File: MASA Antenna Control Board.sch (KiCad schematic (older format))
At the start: 10 parts

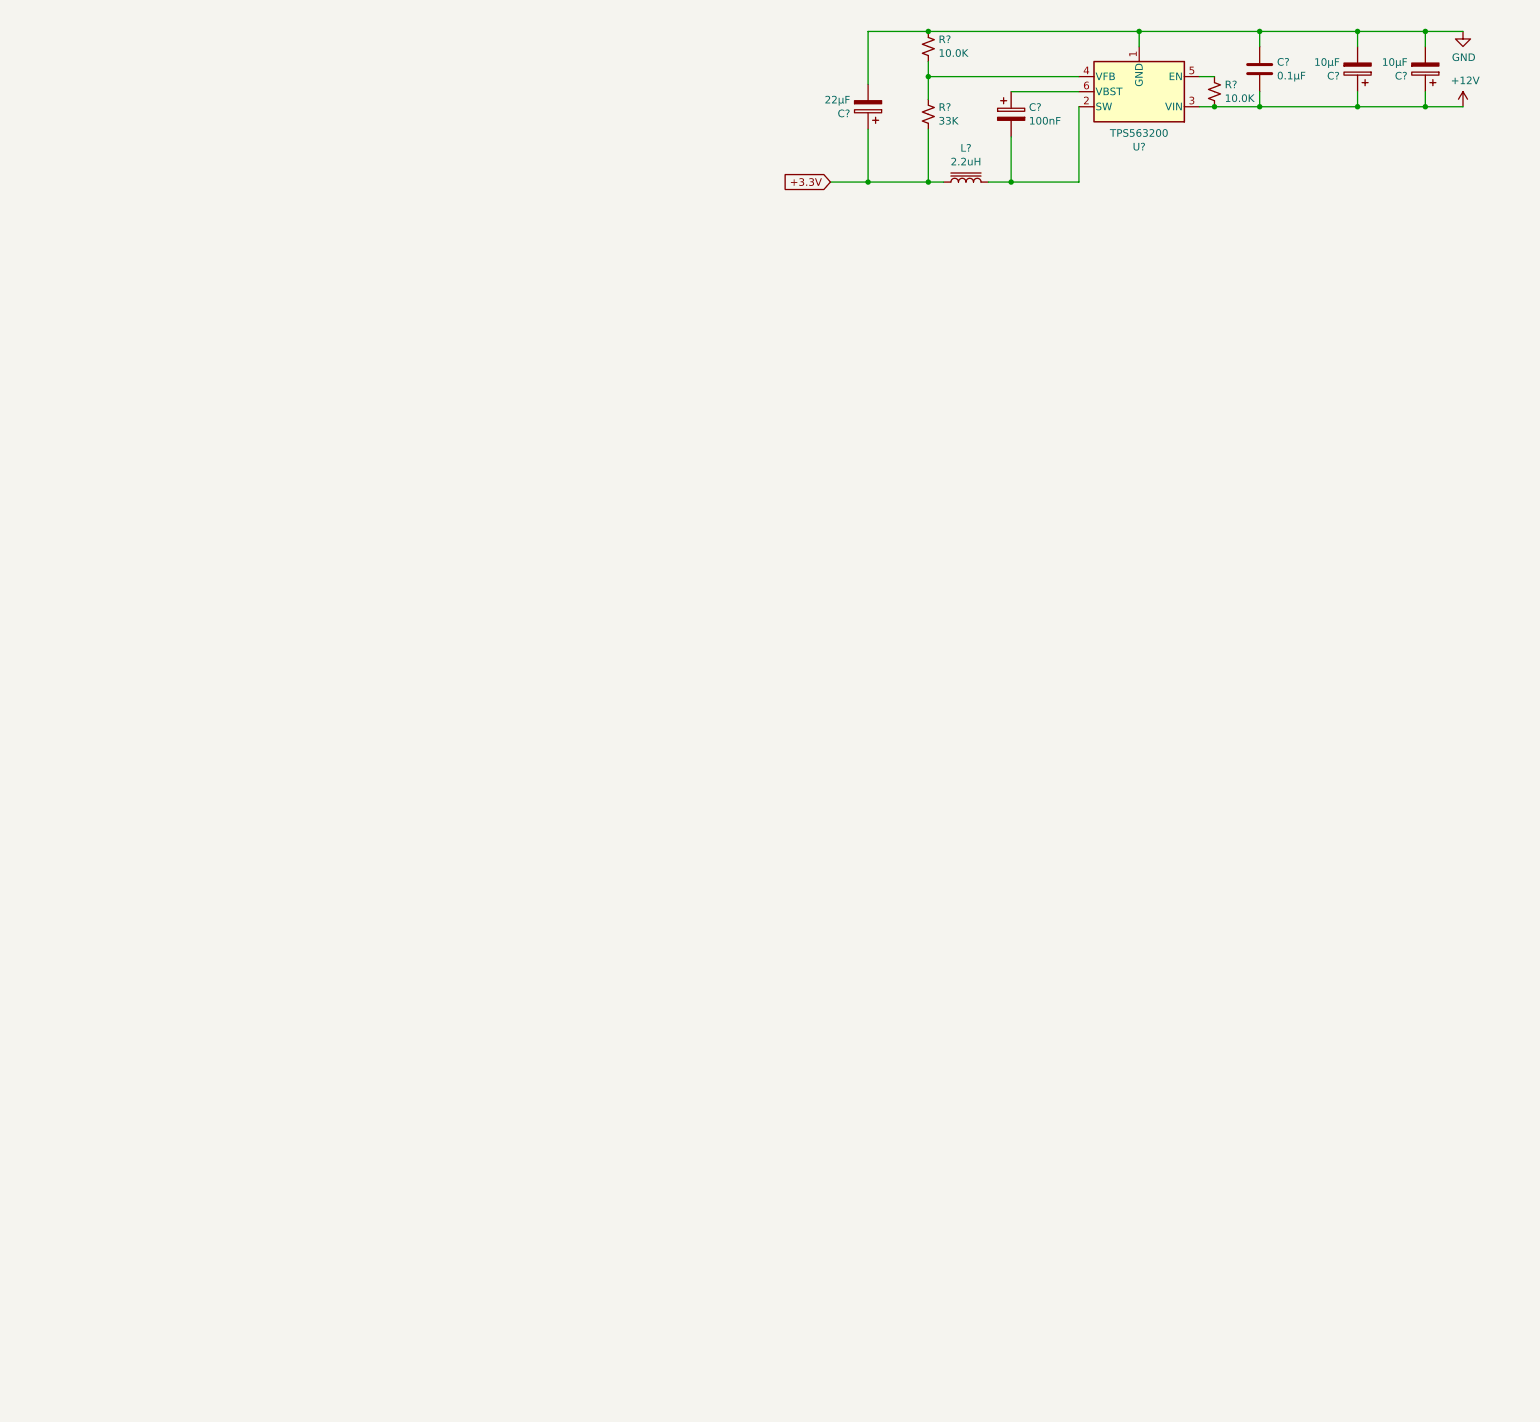
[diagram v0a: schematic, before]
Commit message: Finished schematic and assigned footprints
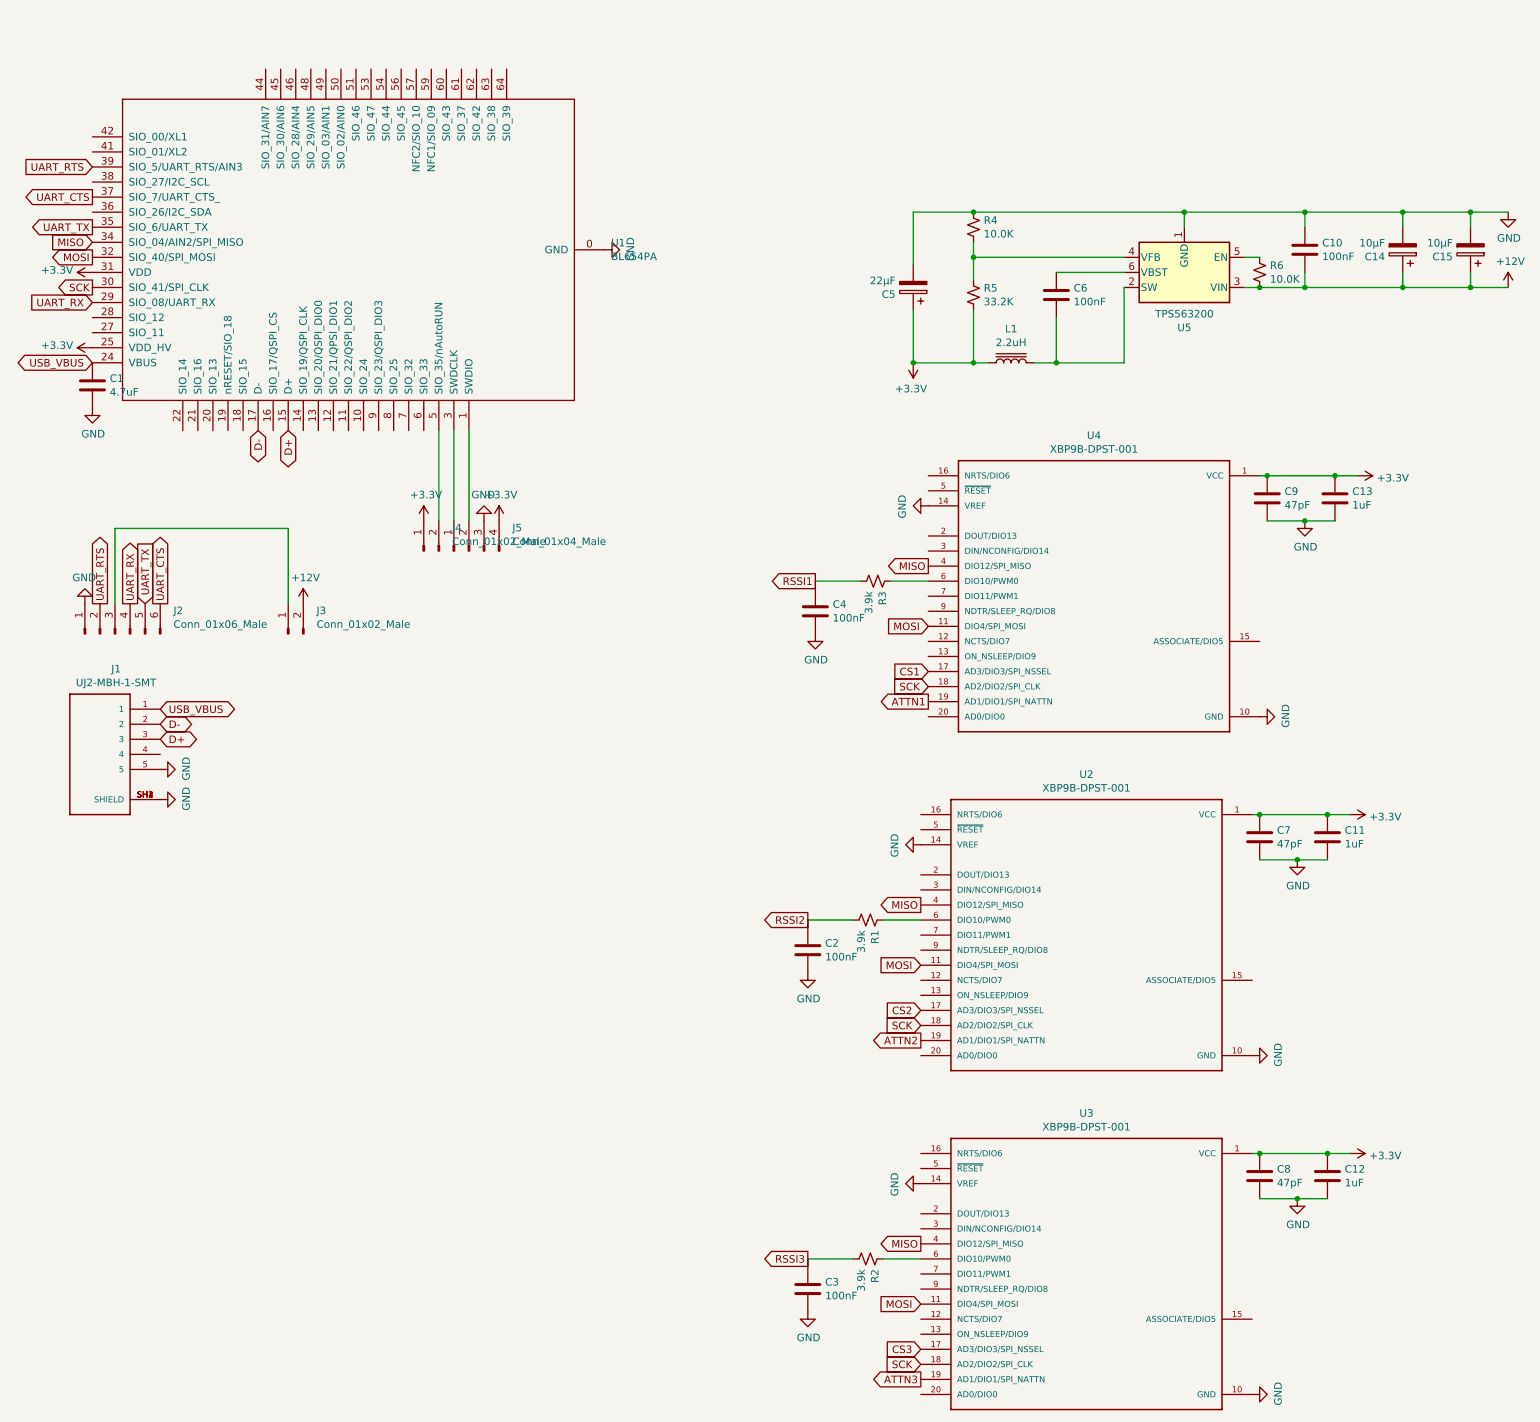
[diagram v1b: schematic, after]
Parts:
- removed C?: 100nF, symbol Device:CP
- added C1: 4.7uF, Capacitor_SMD:C_0805_2012Metric, symbol Device:C
- added C11, C12, C13: 1uF, Capacitor_SMD:C_0805_2012Metric, symbol Device:C
- added C2, C3, C4, C6: 100nF, Capacitor_SMD:C_0805_2012Metric, symbol Device:C
- added C7, C8, C9: 47pF, Capacitor_SMD:C_0805_2012Metric, symbol Device:C
- added J1: UJ2-MBH-1-SMT, Tracking-Antenna-Control-Board:CUI_UJ2-MBH-1-SMT, symbol UJ2-MBH-1-SMT:UJ2-MBH-1-SMT
- added J2: Conn_01x06_Male, Connector_PinSocket_2.54mm:PinSocket_1x06_P2.54mm_Vertical, symbol Connector:Conn_01x06_Male
- added J3, J4: Conn_01x02_Male, Connector_PinSocket_2.54mm:PinSocket_1x02_P2.54mm_Vertical, symbol Connector:Conn_01x02_Male
- added J5: Conn_01x04_Male, Connector_PinSocket_2.54mm:PinSocket_1x04_P2.54mm_Vertical, symbol Connector:Conn_01x04_Male
- added R1, R2, R3: 3.9k, Resistor_SMD:R_0805_2012Metric, symbol Device:R_Small_US
- added U1: BL654PA, MASA_Library:BL654PA, symbol MASA_Library:BL654PA
- added U2, U3, U4: XBP9B-DPST-001, Tracking-Antenna-Control-Board:DIP2200W51P200L3294H279Q20P, symbol XBP9B-DPST-001:XBP9B-DPST-001
- C10: renamed from C?; value 0.1μF -> 100nF; footprint (none) -> Capacitor_SMD:C_0805_2012Metric
- C14, C15, C5: renamed from C?; footprint (none) -> Capacitor_THT:CP_Axial_L11.0mm_D5.0mm_P18.00mm_Horizontal
- L1: renamed from L?; footprint (none) -> Inductor_SMD:L_0805_2012Metric
- R4, R6: renamed from R?; footprint (none) -> Resistor_SMD:R_0805_2012Metric
- R5: renamed from R?; value 33K -> 33.2K; footprint (none) -> Resistor_SMD:R_0805_2012Metric
- gave numbers to parts that had none: 1
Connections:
- net +12V: now also J3.2 (Pin_2)
- net GND: now also C1.2, C11.2, C12.2, C13.2, C2.2, C3.2, C4.2, C7.2, C8.2, C9.2, J1.5, J1.SH1 (SHIELD), J1.SH2 (SHIELD), J1.SH3 (SHIELD), J1.SH4 (SHIELD), J2.1 (Pin_1), J5.3 (Pin_3), U1.0 (GND), U1.23 (GND), U1.26 (GND), U1.33 (GND), U1.40 (GND), U1.43 (GND), U1.47 (GND), U1.52 (GND), U1.55 (GND), U1.58 (GND), U1.65 (GND), U1.66 (GND), U1.67 (GND), U1.68 (GND), U1.69 (GND), U1.70 (GND), U1.71 (GND), U1.72 (GND), U1.73 (GND), U1.74 (GND), U1.75 (GND), U1.76 (GND), U1.77 (GND), U1.78 (GND), U1.79 (GND), U2.10 (GND), U2.14 (VREF), U3.10 (GND), U3.14 (VREF), U4.10 (GND), U4.14 (VREF)
- net at L1.2, U5.2 (SW): now also C6.2
- net at U5.6 (VBST): now also C6.1
- net +3.3V renamed +3V3
- net +3V3: now also C11.1, C12.1, C13.1, C7.1, C8.1, C9.1, J4.1 (Pin_1), J5.4 (Pin_4), U1.25 (VDD_HV), U1.31 (VDD), U2.1 (VCC), U3.1 (VCC), U4.1 (VCC)
- new net: J5.2 (Pin_2), U1.1 (SWDIO)
- new net: J5.1 (Pin_1), U1.3 (SWDCLK)
- new net: J4.2 (Pin_2), U1.5 (SIO_35/nAutoRUN)
- new net: J2.3 (Pin_3), J3.1 (Pin_1)
- new net: R3.1, U4.6 (DIO10/PWM0)
- new net: R1.1, U2.6 (DIO10/PWM0)
- new net: R2.1, U3.6 (DIO10/PWM0)
- new net ATTN1: U4.19 (AD1/DIO1/SPI_NATTN)
- new net ATTN2: U2.19 (AD1/DIO1/SPI_NATTN)
- new net ATTN3: U3.19 (AD1/DIO1/SPI_NATTN)
- new net CS1: U4.17 (AD3/DIO3/SPI_NSSEL)
- new net CS2: U2.17 (AD3/DIO3/SPI_NSSEL)
- new net CS3: U3.17 (AD3/DIO3/SPI_NSSEL)
- new net D+: J1.3, U1.15 (D+)
- new net D-: J1.2, U1.17 (D-)
- new net MISO: U1.34 (SIO_04/AIN2/SPI_MISO), U2.4 (DIO12/SPI_MISO), U3.4 (DIO12/SPI_MISO), U4.4 (DIO12/SPI_MISO)
- new net MOSI: U1.32 (SIO_40/SPI_MOSI), U2.11 (DIO4/SPI_MOSI), U3.11 (DIO4/SPI_MOSI), U4.11 (DIO4/SPI_MOSI)
- new net RSSI1: C4.1, R3.2
- new net RSSI2: C2.1, R1.2
- new net RSSI3: C3.1, R2.2
- new net SCK: U1.30 (SIO_41/SPI_CLK), U2.18 (AD2/DIO2/SPI_CLK), U3.18 (AD2/DIO2/SPI_CLK), U4.18 (AD2/DIO2/SPI_CLK)
- new net UART_CTS: J2.6 (Pin_6), U1.37 (SIO_7/UART_CTS_)
- new net UART_RTS: J2.2 (Pin_2), U1.39 (SIO_5/UART_RTS/AIN3)
- new net UART_RX: J2.4 (Pin_4), U1.29 (SIO_08/UART_RX)
- new net UART_TX: J2.5 (Pin_5), U1.35 (SIO_6/UART_TX)
- new net USB_VBUS: C1.1, J1.1, U1.24 (VBUS)
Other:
- moved on the sheet: C10, C14, C15, C5, L1, R4, R5, R6, U5

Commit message: Finished most routing
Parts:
- C14, C15, C5: footprint Capacitor_THT:CP_Axial_L11.0mm_D5.0mm_P18.00mm_Horizontal -> Capacitor_THT:CP_Radial_D5.0mm_P2.00mm
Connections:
- net ATTN1: now also U1.21 (SIO_16)
- net ATTN2: now also U1.53 (SIO_47)
- net CS1: now also U1.14 (SIO_19/QSPI_CLK)
- net CS2: now also U1.51 (SIO_46)
- net RSSI1: now also U1.45 (SIO_30/AIN6)
- net RSSI2: now also U1.49 (SIO_03/AIN1)
- net RSSI3: now also U1.50 (SIO_02/AIN0)
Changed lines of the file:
@@
 F 0 "C15" H 10818 2396 50  0000 L CNN
 F 1 "10μF" H 10818 2305 50  0000 L CNN
-F 2 "Capacitor_THT:CP_Axial_L11.0mm_D5.0mm_P18.00mm_Horizontal" H 10738 2200 50  0001 C CNN
+F 2 "Capacitor_THT:CP_Radial_D5.0mm_P2.00mm" H 10738 2200 50  0001 C CNN
 F 3 "~" H 10700 2350 50  0001 C CNN
 	1    10700 2350
@@
 F 0 "C14" H 10368 2396 50  0000 L CNN
 F 1 "10μF" H 10368 2305 50  0000 L CNN
-F 2 "Capacitor_THT:CP_Axial_L11.0mm_D5.0mm_P18.00mm_Horizontal" H 10288 2200 50  0001 C CNN
+F 2 "Capacitor_THT:CP_Radial_D5.0mm_P2.00mm" H 10288 2200 50  0001 C CNN
 F 3 "~" H 10250 2350 50  0001 C CNN
 	1    10250 2350
@@
 F 0 "C5" H 7118 2646 50  0000 L CNN
 F 1 "22μF" H 7118 2555 50  0000 L CNN
-F 2 "Capacitor_THT:CP_Axial_L11.0mm_D5.0mm_P18.00mm_Horizontal" H 7038 2450 50  0001 C CNN
+F 2 "Capacitor_THT:CP_Radial_D5.0mm_P2.00mm" H 7038 2450 50  0001 C CNN
 F 3 "~" H 7000 2600 50  0001 C CNN
 	1    7000 2600
@@
 	0    -1   -1   0
 $EndComp
+Text GLabel 3100 1150 1    50   Input ~ 0
+RSSI2
+Text GLabel 2800 1150 1    50   Input ~ 0
+RSSI1
+Text GLabel 3200 1150 1    50   Input ~ 0
+RSSI3
+Text GLabel 3300 1150 1    50   Output ~ 0
+CS2
+Text GLabel 3400 1150 1    50   Output ~ 0
+ATTN2
+Text GLabel 2250 3550 3    50   Input ~ 0
+ATTN1
+Text GLabel 2950 3550 3    50   Input ~ 0
+CS1
 $EndSCHEMATC

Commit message: Finished routing
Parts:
- added J6, J7, J8: 1-1123723-2, TE_1-1123723-2, symbol 1-1123723-2:1-1123723-2
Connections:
- net +12V: now also J6.1
- net GND: now also J6.2
- net StepperFour: now reaches U1.11 (SIO_22/QSPI_DIO2)
- net StepperFour: now also J8.2
- net StepperThree: now reaches U1.13 (SIO_20/QSPI_DIO0)
- net StepperThree: now also J8.1
- net StepperTwo: now reaches U1.7 (SIO_32)
- net StepperTwo: now also J7.2
- net StepperOne: now reaches U1.9 (SIO_23/QSPI_DIO3)
- net StepperOne: now also J7.1
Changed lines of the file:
@@
 Text GLabel 2950 3550 3    50   Input ~ 0
 CS1
+$Comp
+L 1-1123723-2:1-1123723-2 J6
+U 1 1 5E45F8EE
+P 1500 6600
+F 0 "J6" H 1443 6333 50  0000 C CNN
+F 1 "1-1123723-2" H 1443 6424 50  0000 C CNN
+F 2 "TE_1-1123723-2" H 1500 6600 50  0001 L BNN
+F 3 "1-1123723-2" H 1500 6600 50  0001 L BNN
+F 4 "Header" H 1500 6600 50  0001 L BNN "Field4"
+F 5 "https://www.te.com/usa-en/product-1-1123723-2.html?te_bu=Cor&te_type=disp&te_campaign=seda_glo_cor-seda-global-disp-prtnr-fy19-seda-model-bom-cta_sma-317_1&elqCampaignId=32493" H 1500 6600 50  0001 L BNN "Field5"
+F 6 "2" H 1500 6600 50  0001 L BNN "Field6"
+F 7 "Compliant" H 1500 6600 50  0001 L BNN "Field7"
+F 8 "3.96 mm[.156 in]" H 1500 6600 50  0001 L BNN "Field8"
+	1    1500 6600
+	-1   0    0    1
+$EndComp
+$Comp
+L power:GND #PWR0101
+U 1 1 5E460A14
+P 1700 6600
+F 0 "#PWR0101" H 1700 6350 50  0001 C CNN
+F 1 "GND" V 1705 6472 50  0000 R CNN
+F 2 "" H 1700 6600 50  0001 C CNN
+F 3 "" H 1700 6600 50  0001 C CNN
+	1    1700 6600
+	0    -1   -1   0
+$EndComp
+$Comp
+L power:+12V #PWR0102
+U 1 1 5E46162D
+P 1700 6700
+F 0 "#PWR0102" H 1700 6550 50  0001 C CNN
+F 1 "+12V" V 1715 6828 50  0000 L CNN
+F 2 "" H 1700 6700 50  0001 C CNN
+F 3 "" H 1700 6700 50  0001 C CNN
+	1    1700 6700
+	0    1    1    0
+$EndComp
+$Comp
+L 1-1123723-2:1-1123723-2 J7
+U 1 1 5E4652DA
+P 1500 7150
+F 0 "J7" H 1443 6883 50  0000 C CNN
+F 1 "1-1123723-2" H 1443 6974 50  0000 C CNN
+F 2 "TE_1-1123723-2" H 1500 7150 50  0001 L BNN
+F 3 "1-1123723-2" H 1500 7150 50  0001 L BNN
+F 4 "Header" H 1500 7150 50  0001 L BNN "Field4"
+F 5 "https://www.te.com/usa-en/product-1-1123723-2.html?te_bu=Cor&te_type=disp&te_campaign=seda_glo_cor-seda-global-disp-prtnr-fy19-seda-model-bom-cta_sma-317_1&elqCampaignId=32493" H 1500 7150 50  0001 L BNN "Field5"
+F 6 "2" H 1500 7150 50  0001 L BNN "Field6"
+F 7 "Compliant" H 1500 7150 50  0001 L BNN "Field7"
+F 8 "3.96 mm[.156 in]" H 1500 7150 50  0001 L BNN "Field8"
+	1    1500 7150
+	-1   0    0    1
+$EndComp
+$Comp
+L 1-1123723-2:1-1123723-2 J8
+U 1 1 5E465BF1
+P 1500 7700
+F 0 "J8" H 1443 7433 50  0000 C CNN
+F 1 "1-1123723-2" H 1443 7524 50  0000 C CNN
+F 2 "TE_1-1123723-2" H 1500 7700 50  0001 L BNN
+F 3 "1-1123723-2" H 1500 7700 50  0001 L BNN
+F 4 "Header" H 1500 7700 50  0001 L BNN "Field4"
+F 5 "https://www.te.com/usa-en/product-1-1123723-2.html?te_bu=Cor&te_type=disp&te_campaign=seda_glo_cor-seda-global-disp-prtnr-fy19-seda-model-bom-cta_sma-317_1&elqCampaignId=32493" H 1500 7700 50  0001 L BNN "Field5"
+F 6 "2" H 1500 7700 50  0001 L BNN "Field6"
+F 7 "Compliant" H 1500 7700 50  0001 L BNN "Field7"
+F 8 "3.96 mm[.156 in]" H 1500 7700 50  0001 L BNN "Field8"
+	1    1500 7700
+	-1   0    0    1
+$EndComp
+Text GLabel 1700 7250 2    50   Output ~ 0
+StepperOne
+Text GLabel 1700 7150 2    50   Output ~ 0
+StepperTwo
+Text GLabel 1700 7800 2    50   Output ~ 0
+StepperThree
+Text GLabel 1700 7700 2    50   Output ~ 0
+StepperFour
+Text GLabel 3650 3550 3    50   Output ~ 0
+StepperTwo
+Text GLabel 3450 3550 3    50   Output ~ 0
+StepperOne
+Text GLabel 3250 3550 3    50   Output ~ 0
+StepperFour
+Text GLabel 3050 3550 3    50   Output ~ 0
+StepperThree
 $EndSCHEMATC
